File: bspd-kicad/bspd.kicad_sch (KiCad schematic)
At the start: 52 parts, among them J1 BSPD Connector, Q1 AO3400A, U1 MCP1703T-5002E/CB, U7 SN74LVC2G14DBVR, U8 74HC74

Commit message: Fixed latch and added indicator LEDs
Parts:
- removed C10: 2.2uF, Capacitor_SMD:C_0805_2012Metric_Pad1.18x1.45mm_HandSolder, symbol Device:C
- removed Q1: AO3400A, Package_TO_SOT_SMD:SOT-23, symbol Transistor_FET:AO3400A
- removed U8: 74HC74, Package_SO:SOIC-14-16_3.9x9.9mm_P1.27mm, symbol 74xx:74HC74
- added C11: 5uF, Capacitor_SMD:C_0805_2012Metric_Pad1.18x1.45mm_HandSolder, symbol Device:C
- added D10, D11, D5, D6, D7, D8, D9: AP2012EC, bspd:AP2012EC, symbol bspd:AP2012EC
- added Q2: AO3401A, Package_TO_SOT_SMD:SOT-23, symbol Transistor_FET:AO3401A
- added R30: 150k, Resistor_SMD:R_0805_2012Metric_Pad1.20x1.40mm_HandSolder, symbol Device:R_US
- added R31, R32, R33, R34, R35, R36, R37, R38: 300, Resistor_SMD:R_0805_2012Metric_Pad1.20x1.40mm_HandSolder, symbol Device:R_US
- added RV4, RV5, RV6: 3313J-1-103E, bspd:3313J-1-103E, symbol bspd:3313J-1-103E
- added U6: SN74HC74DR, bspd:SN74HC74DR, symbol bspd:SN74HC74DR
- added U8, U9: SN74LVC3G14DCUR, bspd:SN74LVC3G14DCUR, symbol bspd:SN74LVC3G14DCUR
- R29: value 330k -> 150k
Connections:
- net +12V: now also Q2.2 (S)
- net +5V: now also R30.1, RV4.1, RV5.1, RV6.1, U6.14 (VCC), U8.8 (VCC), U9.8 (VCC); no longer R29.2
- net BPS_FAULT: now also U8.6
- net Earth: now also C11.1, R31.2, R32.2, R33.2, R34.2, R35.2, R36.2, R37.2, RV4.3, RV5.3, RV6.3, U6.10 (~{PRE}), U6.11 (C), U6.12 (D), U6.13 (~{CLR}), U6.2 (D), U6.3 (C), U6.7 (GND), U8.4 (GND), U9.4 (GND)
- net FAULT: now also U6.1 (~{CLR}), U9.6
- net HB_THRESH: now also RV4.2
- net SC_OUT: now also Q2.3 (D)
- net TPS1_FAULT: now also U8.1
- net TPS1_THRESH: now also RV5.2
- net TPS2_FAULT: now also U8.3
- net TPS2_THRESH: now also RV6.2
- net at D4.2 (A), U7.1: now also R29.2, C11.2; no longer R29.1
- net TPSx10%: now reaches R11.2, R13.2, U3.13, U4.2
- net TPSx10%: now also U9.1
- net at U7.4: now also U6.4 (~{PRE})
- net HB: now reaches R11.1, R6.1, U4.7 (+)
- net HB: now also U9.3
- new net: D5.1 (K), R31.1
- new net: D9.1 (K), R35.1
- new net: D8.1 (K), R34.1
- new net: D8.2 (A), U8.2
- new net: D10.1 (K), R36.1
- new net: D10.2 (A), U9.5
- new net: R38.1, U6.5 (Q)
- new net: D7.1 (K), R33.1
- new net: D9.2 (A), U9.7
- new net: D7.2 (A), U8.5
- new net: R29.1, R30.2
- new net: D11.1 (K), R37.1
- new net: D11.2 (A), U9.2
- new net: Q2.1 (G), R38.2
- new net: D6.1 (K), R32.1
- new net: D6.2 (A), U8.7
- new net LATCH_LED: D5.2 (A), U6.6 (~{Q})
- no-connect marks 1 -> 2
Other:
- note added: "Indicator LED"
- note added: "Output Logic"
- note added: "Unused parts of D-latch"
- note added: "Variable Voltage References"
- moved on the sheet: C1, C2, C3, C4, C5, C6, C7, C8, C9, D1, D2, D3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

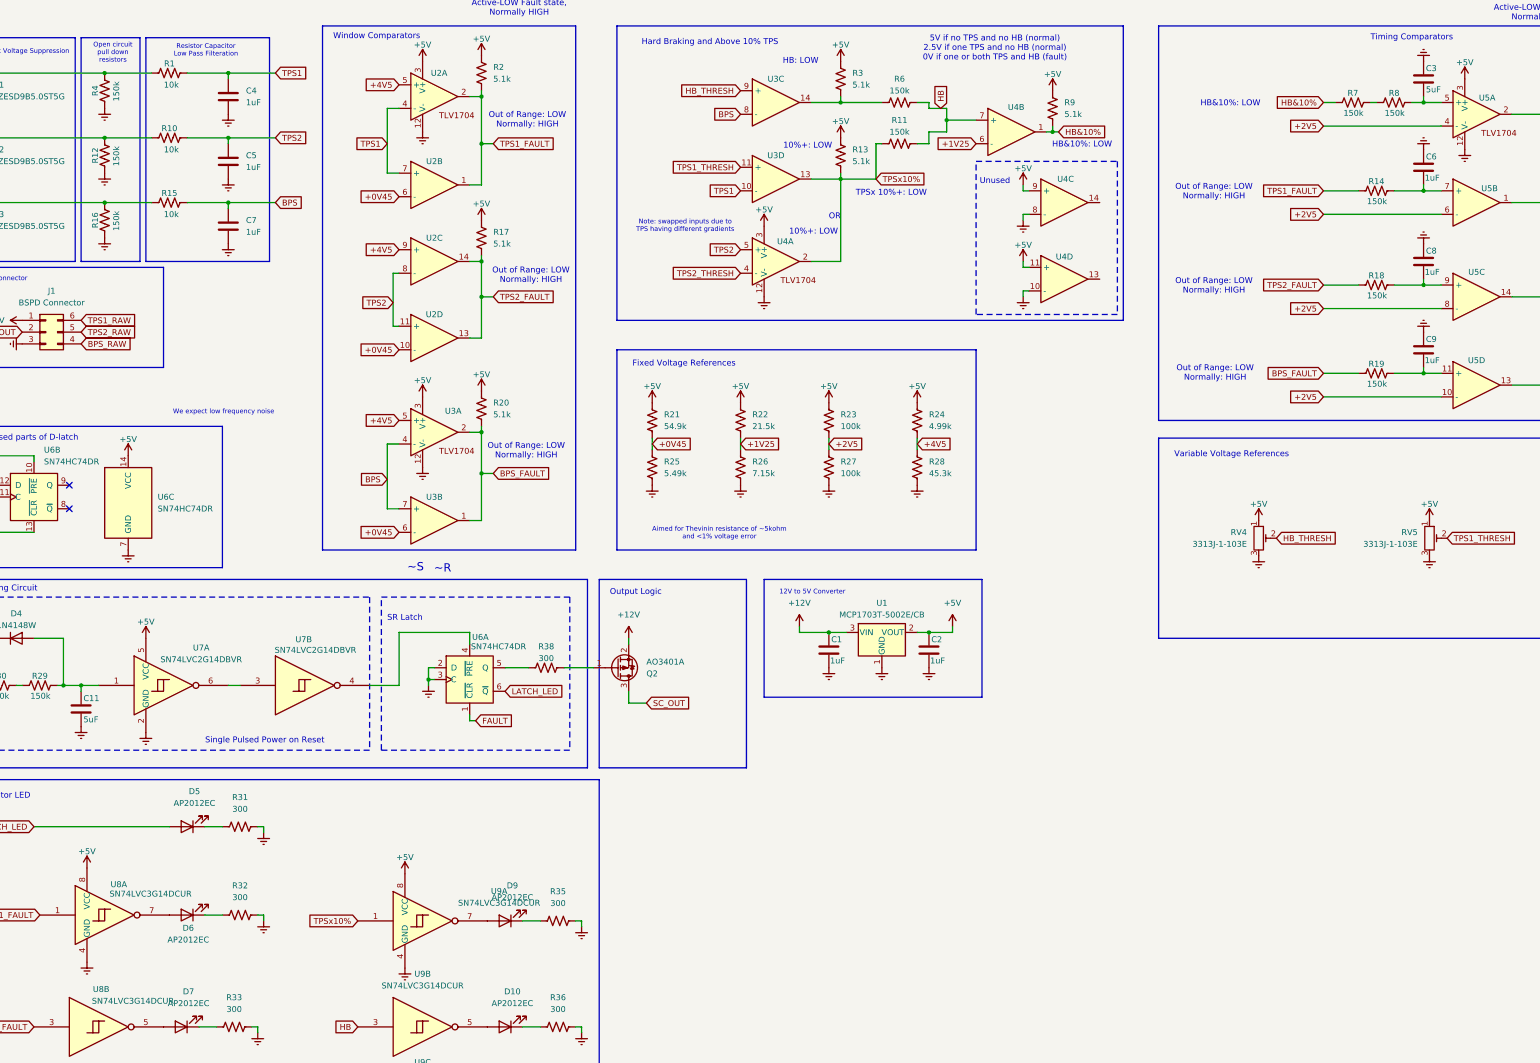
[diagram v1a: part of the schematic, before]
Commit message: Added decoupling
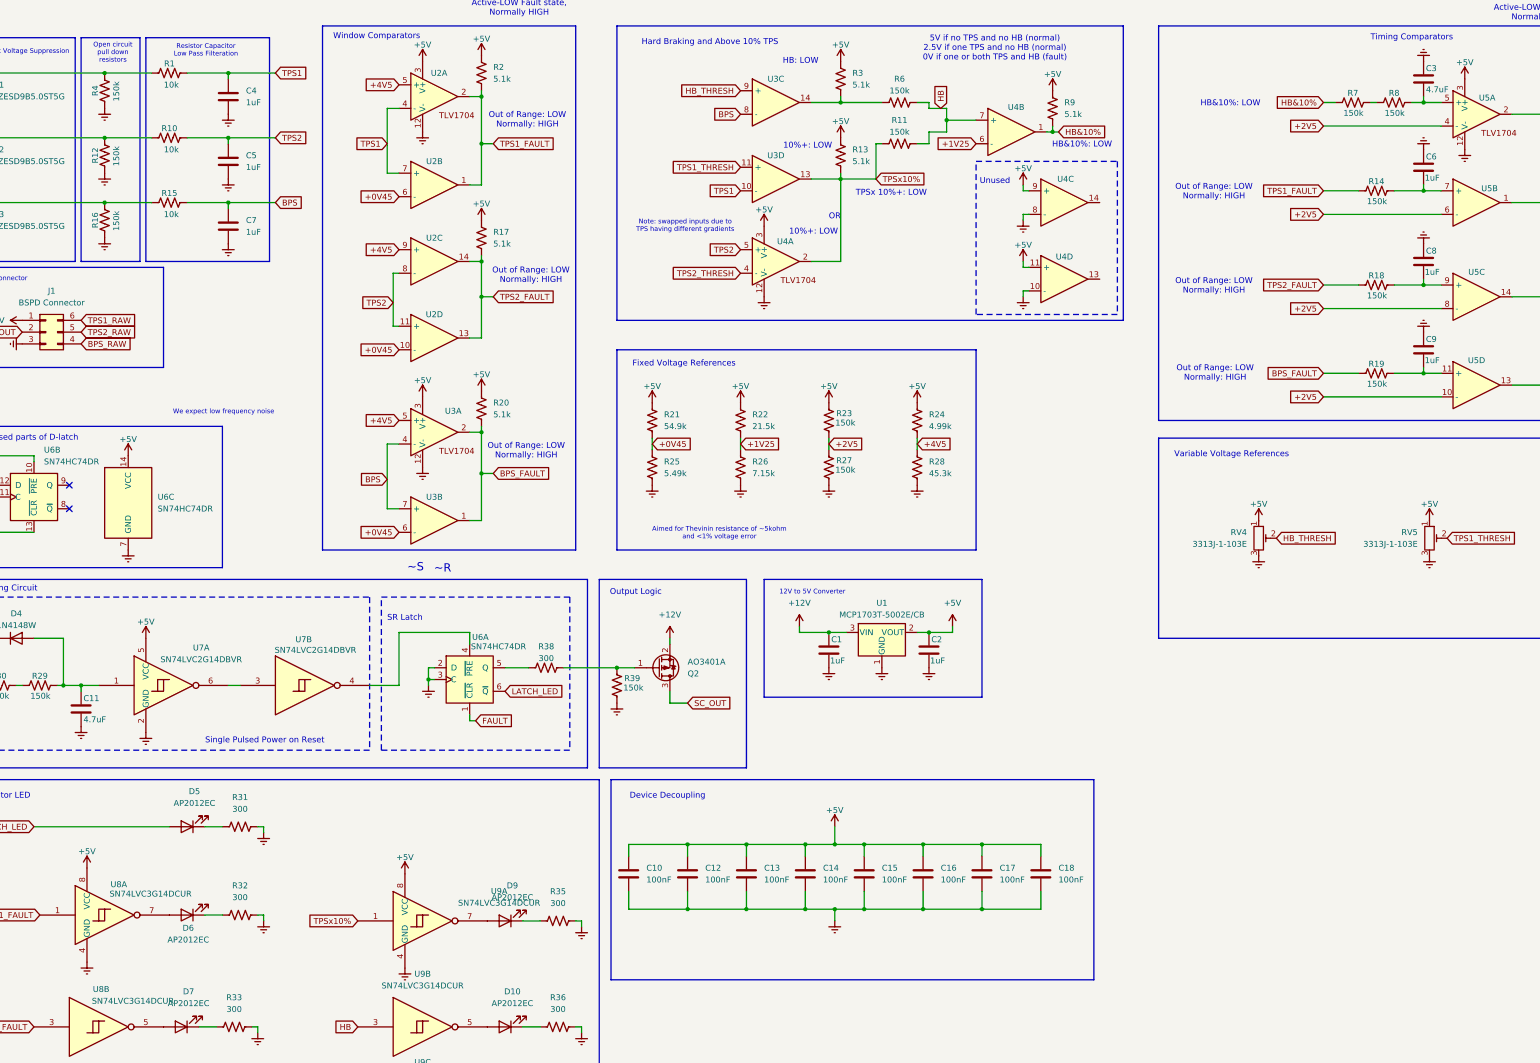
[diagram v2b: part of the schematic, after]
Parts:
- added C10, C12, C13, C14, C15, C16, C17, C18: 100nF, symbol Device:C
- added R39: 150k, Resistor_SMD:R_0805_2012Metric_Pad1.20x1.40mm_HandSolder, symbol Device:R_US
- C11, C3: value 5uF -> 4.7uF
- R23, R27: value 100k -> 150k
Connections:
- net +2V5: now also R23.1, R27.2; no longer R23.2, R27.1
- net +5V: now also R23.2, C10.1, C12.1, C13.1, C14.1, C15.1, C16.1, C17.1, C18.1; no longer R23.1
- net Earth: now also R27.1, C10.2, C12.2, C13.2, C14.2, C15.2, C16.2, C17.2, C18.2, R39.1; no longer R27.2
- net at Q2.1 (G), R38.2: now also R39.2
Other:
- note added: "Device Decoupling"
- moved on the sheet: Q2

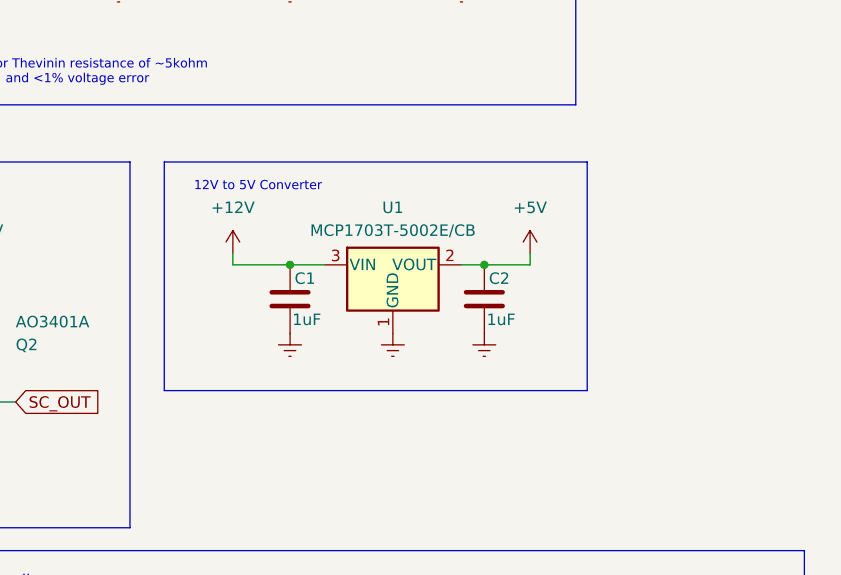
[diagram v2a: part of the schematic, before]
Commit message: TVS for 12V added
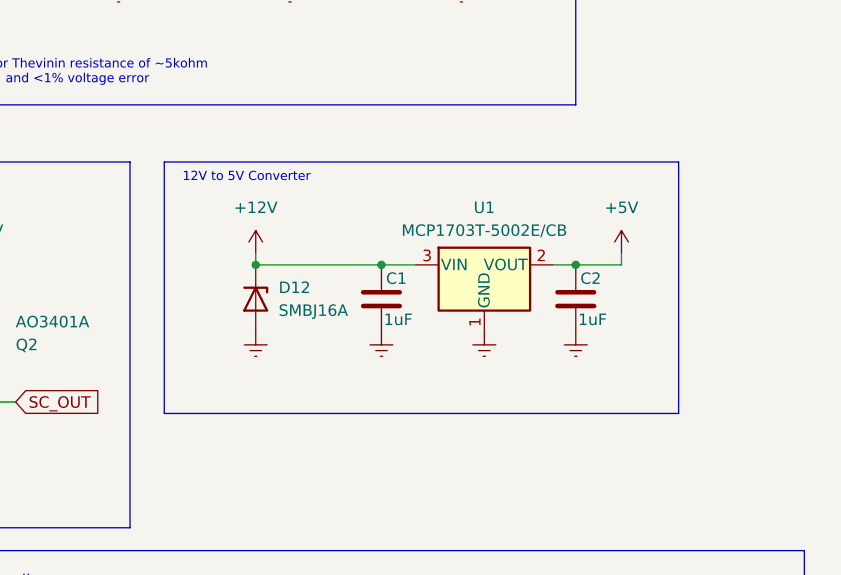
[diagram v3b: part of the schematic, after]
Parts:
- added D12: SMBJ16A, bspd:SMBJ16A, symbol bspd:SMBJ16A
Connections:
- net +12V: now also D12.1 (K)
- net Earth: now also D12.2 (A)
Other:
- moved on the sheet: C1, C2, U1

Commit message: Modified output logic
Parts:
- removed Q2: AO3401A, Package_TO_SOT_SMD:SOT-23, symbol Transistor_FET:AO3401A
- removed R29: 150k, Resistor_SMD:R_0805_2012Metric_Pad1.20x1.40mm_HandSolder, symbol Device:R_US
- added D1: 1N4148W, Diode_SMD:D_SOD-123, symbol Diode:1N4148W
- added Q1: AO3401A, Package_TO_SOT_SMD:SOT-23, symbol Transistor_FET:AO3401A
- added Q2: AO3400A, Package_TO_SOT_SMD:SOT-23, symbol Transistor_FET:AO3400A
- added R31: 150k, Resistor_SMD:R_0805_2012Metric_Pad1.20x1.40mm_HandSolder, symbol Device:R_US
- added R40: 56k, Resistor_SMD:R_0805_2012Metric_Pad1.20x1.40mm_HandSolder, symbol Device:R_US
- added RV4, RV5: 3313J-1-203E, bspd:3313J-1-103E, symbol bspd:3313J-1-103E
- added SW1, SW2: CJS-1200TB1, bspd:CJS-1200TB1, symbol bspd:CJS-1200TB1
- R39: value 150k -> 47k
- RV1: renamed from RV4; value 3313J-1-103E -> 3313J-1-203E
- RV2: renamed from RV5; value 3313J-1-103E -> 3313J-1-203E
- RV3: renamed from RV6; value 3313J-1-103E -> 3313J-1-203E
- renumbered C3 to C1, C11 to C10, C10 to C11, C4 to C2, C5 to C3, C6 to C4, C7 to C5, C8 to C6, C9 to C7, C1 to C8, C2 to C9, D7 to D10, D10 to D11, D11 to D12, D8 to D13, D1 to D2, D2 to D3, D3 to D4, D4 to D5, D12 to D6, D5 to D7, D6 to D8, R38 to R29, R31 to R32, R32 to R33, R35 to R34, R33 to R35, R34 to R38, U2 to U1, U3 to U2, U5 to U3, U6 to U5, U1 to U6
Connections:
- net +0V45: now also SW1.3 (C); no longer U1.10 (-), U1.6 (-), U2.6 (-)
- net +12V: now also Q1.2 (S), R40.2
- net +4V5: now also SW2.3 (C); no longer U1.5 (+), U1.9 (+), U2.5 (+)
- net +5V: now also RV4.1, RV5.1
- net Earth: now also Q2.2 (S), R31.1, RV4.3, RV5.3; no longer R39.1
- net HB: now also R3.2, R6.2, U2.14; no longer R11.1, R6.1, U4.7 (+)
- net HB&10%: now also D1.2 (A)
- net SC_OUT: now also Q1.3 (D)
- net at R39.2: now also Q1.1 (G), R40.1; no longer R29.2
- net at C10.2, D5.2 (A), U7.1: now also R30.2
- net at C1.1, R8.2, U3.5 (+): now also D1.1 (K)
- new net: Q2.1 (G), R29.2, R31.2
- new net: R11.1, R6.1, U4.7 (+)
- new net: Q2.3 (D), R39.1
- new net V_THH: SW2.2 (B), U1.5 (+), U1.9 (+), U2.5 (+)
- new net V_THH_VAR: RV5.2, SW2.1 (A)
- new net V_THL: SW1.2 (B), U1.10 (-), U1.6 (-), U2.6 (-)
- new net V_THL_VAR: RV4.2, SW1.1 (A)
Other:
- note added: "20k trim pots"
- note added: "Switch Fixed/Variable References"
- moved on the sheet: C8, C9, D6, R7, R8, RV1, RV2, RV3, U6

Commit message: Started layout, emphasis on looking good
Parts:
- removed U6: MCP1703T-5002E/CB, bspd:MCP1703T-5002E-CB, symbol bspd:MCP1703T-5002E-CB
- added C19: 4.7uF, Capacitor_SMD:C_0805_2012Metric_Pad1.18x1.45mm_HandSolder, symbol Device:C
- added C20, C21, C22, C23, C24, C25, C26, C27, C28: 100nF, Capacitor_SMD:C_0805_2012Metric_Pad1.18x1.45mm_HandSolder, symbol Device:C
- added D14: 1N4148W, Diode_SMD:D_SOD-123, symbol Diode:1N4148W
- added U10: LM1117MP-5.0, Package_TO_SOT_SMD:SOT-223-3_TabPin2, symbol Regulator_Linear:LM1117MP-5.0
- C11, C12, C13, C14, C15, C16, C17, C18: footprint (none) -> Capacitor_SMD:C_0805_2012Metric_Pad1.18x1.45mm_HandSolder
- C8, C9: value 1uF -> 10uF
- R29, R32, R33, R34, R35, R36, R37, R38: value 300 -> 500
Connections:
- net +0V45: now also C25.1
- net +12V: now also D14.1 (K), U10.3 (VI)
- net +1V25: now also C26.1
- net +2V5: now also C27.1
- net +4V5: now also C28.1
- net +5V: now also U5.10 (~{PRE}), U5.13 (~{CLR}), U10.2 (VO)
- net Earth: now also C19.1, C20.2, C21.2, C22.2, C23.2, C24.2, C25.2, C26.2, C27.2, C28.2, U10.1 (GND); no longer U5.10 (~{PRE}), U5.13 (~{CLR})
- net HB_THRESH: now also C21.1
- net SC_OUT: now also D14.2 (A)
- net TPS1_THRESH: now also C22.1
- net TPS2_THRESH: now also C23.1
- net V_THH_VAR: now also C24.1
- net V_THL_VAR: now also C20.1
- net at C10.2, D5.2 (A), R30.2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: now also C19.2
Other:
- moved on the sheet: C11, C12, C13, C14, C15, C16, C17, C18, Q1, Q2, R21, R22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

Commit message: Layout progress
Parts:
- added TP1: TPS1, TestPoint:TestPoint_Keystone_5000-5004_Miniature, symbol Connector:TestPoint
- added TP2: TPS2, TestPoint:TestPoint_Keystone_5000-5004_Miniature, symbol Connector:TestPoint
- added TP3: BPS, TestPoint:TestPoint_Keystone_5000-5004_Miniature, symbol Connector:TestPoint
- added TP4: +0V45, TestPoint:TestPoint_Keystone_5000-5004_Miniature, symbol Connector:TestPoint
- added TP5: +1V25, TestPoint:TestPoint_Keystone_5000-5004_Miniature, symbol Connector:TestPoint
- added TP6: +2V5, TestPoint:TestPoint_Keystone_5000-5004_Miniature, symbol Connector:TestPoint
- added TP7: +4V5, TestPoint:TestPoint_Keystone_5000-5004_Miniature, symbol Connector:TestPoint
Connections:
- net +0V45: now also TP4.1
- net +1V25: now also U4.10 (-), TP5.1; no longer U4.6 (-)
- net +2V5: now also TP6.1
- net +4V5: now also TP7.1
- net +5V: now also U2.11 (+), U2.9 (+); no longer U4.11 (+), U4.9 (+)
- net BPS: now also U4.4 (-), TP3.1; no longer U2.8 (-)
- net Earth: now also U2.10 (-), U2.8 (-); no longer U4.10 (-), U4.8 (-)
- net HB: now also U4.2; no longer U2.14
- net HB&10%: now also U4.13; no longer U4.1
- net HB_THRESH: now also U4.5 (+); no longer U2.9 (+)
- net TPS1: now also U4.6 (-), TP1.1; no longer U2.10 (-)
- net TPS1_THRESH: now also U4.7 (+); no longer U2.11 (+)
- net TPS2: now also U4.9 (+), TP2.1; no longer U4.5 (+)
- net TPS2_THRESH: now also U4.8 (-); no longer U4.4 (-)
- net TPSx10%: now also U4.1, U4.14; no longer U2.13, U4.2
- net at R11.1, R6.1: now also U4.11 (+); no longer U4.7 (+)
- no-connect marks 2 -> 4

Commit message: Progress
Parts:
- removed D14: 1N4148W, Diode_SMD:D_SOD-123, symbol Diode:1N4148W
- added D15: SS14, Diode_SMD:D_SMA, symbol Diode:SS14
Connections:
- net +12V: now also D15.1 (K)
- net SC_OUT: now also D15.2 (A)
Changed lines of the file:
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@@
 	)
 	(symbol
-		(lib_id "Diode:1N4148W")
-		(at 231.14 171.45 270)
-		(unit 1)
-		(body_style 1)
-		(exclude_from_sim no)
-		(in_bom yes)
-		(on_board yes)
-		(in_pos_files yes)
-		(dnp no)
-		(property "Reference" "D14"
-			(at 236.474 171.45 0)
-			(show_name no)
-			(do_not_autoplace no)
-			(effects
-				(font
-					(size 1.27 1.27)
-				)
-			)
-		)
-		(property "Value" "1N4148W"
-			(at 233.934 171.45 0)
-			(show_name no)
-			(do_not_autoplace no)
-			(effects
-				(font
-					(size 1.27 1.27)
-				)
-			)
-		)
-		(property "Footprint" "Diode_SMD:D_SOD-123"
-			(at 226.695 171.45 0)
-			(hide yes)
-			(show_name no)
-			(do_not_autoplace no)
-			(effects
-				(font
-					(size 1.27 1.27)
-				)
-			)
-		)
-		(property "Datasheet" "https://www.vishay.com/docs/85748/1n4148w.pdf"
-			(at 231.14 171.45 0)
-			(hide yes)
-			(show_name no)
-			(do_not_autoplace no)
-			(effects
-				(font
-					(size 1.27 1.27)
-				)
-			)
-		)
-		(property "Description" "75V 0.15A Fast Switching Diode, SOD-123"
-			(at 231.14 171.45 0)
-			(hide yes)
-			(show_name no)
-			(do_not_autoplace no)
-			(effects
-				(font
-					(size 1.27 1.27)
-				)
-			)
-		)
-		(property "Sim.Device" "D"
-			(at 231.14 171.45 0)
-			(hide yes)
-			(show_name no)
-			(do_not_autoplace no)
-			(effects
-				(font
-					(size 1.27 1.27)
-				)
-			)
-		)
-		(property "Sim.Pins" "1=K 2=A"
-			(at 231.14 171.45 0)
-			(hide yes)
-			(show_name no)
-			(do_not_autoplace no)
-			(effects
-				(font
-					(size 1.27 1.27)
-				)
-			)
-		)
-		(pin "2"
-		)
-		(pin "1"
-		)
-		(instances
-			(project "bspd"
-				(path "/e8b8835b-5dd0-46e2-9a0c-fed9bbaa86de"
-					(reference "D14")
-					(unit 1)
-				)
-			)
-		)
-	)
-	(symbol
 		(lib_id "power:Earth")
 		(at 434.34 139.7 0)
@@
 					(unit 1)
 				)
+			)
+		)
+	)
+	(symbol
+		(lib_id "Diode:SS14")
+		(at 231.14 171.45 270)
+		(unit 1)
+		(body_style 1)
+		(exclude_from_sim no)
+		(in_bom yes)
+		(on_board yes)
+		(in_pos_files yes)
+		(dnp no)
+		(fields_autoplaced yes)
+		(property "Reference" "D15"
+			(at 233.68 169.8624 90)
+			(show_name no)
+			(do_not_autoplace no)
+			(effects
+				(font
+					(size 1.27 1.27)
+				)
+				(justify left)
+			)
+		)
+		(property "Value" "SS14"
+			(at 233.68 172.4024 90)
+			(show_name no)
+			(do_not_autoplace no)
+			(effects
+				(font
+					(size 1.27 1.27)
+				)
+				(justify left)
+			)
+		)
+		(property "Footprint" "Diode_SMD:D_SMA"
+			(at 226.695 171.45 0)
+			(hide yes)
+			(show_name no)
+			(do_not_autoplace no)
+			(effects
+				(font
+					(size 1.27 1.27)
+				)
+			)
+		)
+		(property "Datasheet" "https://www.vishay.com/docs/88746/ss12.pdf"
+			(at 231.14 171.45 0)
+			(hide yes)
+			(show_name no)
+			(do_not_autoplace no)
+			(effects
+				(font
+					(size 1.27 1.27)
+				)
+			)
+		)
+		(property "Description" "40V 1A Schottky Diode, SMA"
+			(at 231.14 171.45 0)
+			(hide yes)
+			(show_name no)
+			(do_not_autoplace no)
+			(effects
+				(font
+					(size 1.27 1.27)
+				)
+			)
+		)
+		(pin "1"
+		)
+		(pin "2"
+		)
+		(instances
+			(project "bspd"
+				(path "/e8b8835b-5dd0-46e2-9a0c-fed9bbaa86de"
+					(reference "D15")
+					(unit 1)
+				)

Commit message: Layout Progress
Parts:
- removed D15: SS14, Diode_SMD:D_SMA, symbol Diode:SS14
- added D7, D8: S1B-13-F, bspd:S1B-13-F, symbol bspd:S1B-13-F
- added R34, R35, R36, R37, R38: 10M, Resistor_SMD:R_0805_2012Metric_Pad1.20x1.40mm_HandSolder, symbol Device:R_US
- R24: value 4.99k -> 2.61k
- R28: value 45.3k -> 49.9k
- renumbered C27 to C10, C28 to C11, C23 to C12, C21 to C13, C22 to C14, C8 to C15, C9 to C16, C20 to C17, C24 to C18, C10 to C20, C11 to C21, C12 to C22, C13 to C23, C14 to C24, C15 to C25, C16 to C26, C17 to C27, C18 to C28, C25 to C8, C26 to C9, D8 to D10, D9 to D11, D10 to D12, D11 to D13, D12 to D14, D13 to D15, D6 to D5, D5 to D6, D7 to D9, Q2 to Q1, Q1 to Q2, R39 to R29, R40 to R30, R29 to R31, R30 to R32, R31 to R33, R32 to R39, R33 to R40, R34 to R41, R35 to R42, R36 to R43, R37 to R44, R38 to R45, U4 to U2, U2 to U4, U10 to U6
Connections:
- net +12V: now also D7.1 (K)
- net +5V: now also R37.2, R38.2
- net Earth: now also D8.2 (A), R34.1, R35.1, R36.1
- net HB_THRESH: now also R34.2
- net SC_OUT: now also D7.2 (A), D8.1 (K)
- net TPS1_THRESH: now also R35.2
- net TPS2_THRESH: now also R37.1
- net V_THH_VAR: now also R36.2
- net V_THL_VAR: now also R38.1
- net OUTPUT: now reaches Q1.1 (G), R31.2, R33.2
- net +4V5 renamed +4V7
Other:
- note added: "Pull up resistors, to mitigate mechanical failture of potentiometers"
- moved on the sheet: C21, C22, C23, C24, C25, C26, C27, C28, Q1, Q2, R29, R30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
